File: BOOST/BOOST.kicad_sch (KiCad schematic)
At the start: 274 parts, among them M1 HYG180N10, M10 HYG180N10, M2 HYG180N10, M3 HYG180N10, M4 HYG180N10, M5 HYG180N10, M6 HYG180N10, M7 HYG180N10, M8 HYG180N10, M9 HYG180N10, Q1 PNP, U1 INA241A3, U10 UCC21520, U11 MCP6241, U12 MCP6241, U13 MCP6241, U14 MCP6561, U15 UCC21520, U16 LM2940_12, U17 L7805, U18 L7805, U19 UCC21520, U2 MCP6561, U20 UCC21520, U21 MCP6561, U22 MCP6241, U23 MCP6241, U24 MCP6241, U3 MCP6241, U4 MCP6561, U5 MCP6561, U6 MCP6241, U7 MCP6241, U8 CD4017B, U9 4051

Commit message: added some footprints to kicad schematic
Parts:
- C1, C39, C4, C56, C73, C79, C80, C81: footprint (none) -> Capacitor_SMD:C_1210_3225Metric
- C10, C11, C12, C13, C14, C15, C17, C19, C20, C22, C23, C24, C26, C28, C29, C32, C33, C34, C35, C36, C37, C38, C41, C42, C43, C44, C45, C46, C47, C48, C5, C50, C51, C52, C53, C54, C58, C59, C61, C63, C65, C66, C68, C8, C82, C83, C84, C9: footprint (none) -> Capacitor_SMD:C_0603_1608Metric
- C16, C18, C49, C60, C64, C67: footprint (none) -> Capacitor_SMD:C_1206_3216Metric
- C2, C21, C25, C27, C3, C31, C57, C6, C62, C72, C76: footprint (none) -> Capacitor_SMD:C_0805_2012Metric
- C30, C55, C7: footprint (none) -> Capacitor_SMD:CP_Elec_6.3x5.4
- C40, C69, C85: footprint (none) -> Capacitor_SMD:CP_Elec_10x12.5
- C70, C71, C74, C75, C77, C78, C86, C87, C88: footprint (none) -> Capacitor_SMD:CP_Elec_10x10.5
- D1, D10, D11, D12, D13, D14, D15, D2, D20, D21, D22, D24, D3, D4, D5, D6, D7, D8, D9: footprint (none) -> Diode_SMD:D_SOD-123
- D19: footprint (none) -> Diode_SMD:D_SMC
- D23, D25, D26: footprint (none) -> Diode_SMD:D_SOD-323
- Q1: footprint (none) -> Package_TO_SOT_SMD:SOT-23
- R1, R52, R53, R7: footprint (none) -> Resistor_SMD:R_2512_6332Metric
- R10, R11, R13, R16, R17, R18, R19, R2, R20, R22, R23, R26, R27, R28, R29, R3, R31, R32, R33, R34, R36, R37, R38, R39, R4, R40, R41, R42, R44, R45, R46, R47, R49, R5, R50, R51, R54, R55, R56, R57, R58, R6, R61, R63, R64, R65, R66, R67, R68, R69, R71, R73, R74, R75, R76, R77, R78, R79, R8, R80, R81, R82, R83, R84, R85, R88, R89, R90, R91, R92, R93, R95, R96, R97, R98: footprint (none) -> Resistor_SMD:R_0603_1608Metric
- R14, R15, R21, R25, R35, R43, R48, R59, R60, R70, R72, R86, R87, R9, R94: footprint (none) -> Resistor_SMD:R_0805_2012Metric
- U1: footprint (none) -> Package_SO:SOIC-8_3.9x4.9mm_P1.27mm
- U10, U15, U19, U20: footprint (none) -> Package_SO:SOIC-16W_7.5x10.3mm_P1.27mm
- U11, U12, U13, U14, U2, U21, U22, U23, U24, U3, U4, U5, U6, U7: footprint (none) -> Package_TO_SOT_SMD:SOT-23-5
- U16: footprint (none) -> Package_TO_SOT_SMD:TO-263-3_TabPin2
- U17, U18: footprint (none) -> Package_TO_SOT_SMD:SOT-89-3
- U8, U9: footprint (none) -> Package_SO:SOIC-16_3.9x9.9mm_P1.27mm
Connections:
- net .1Vref_1: now also D26.1 (-), U3.3 (In+); no longer D26.2 (-), U3.1 (In+)
- net .1Vref_2: now also D25.1 (-), U7.3 (In+); no longer D25.2 (-), U7.1 (In+)
- net .1Vref_3: now also D23.1 (-), U13.3 (In+); no longer D23.2 (-), U13.1 (In+)
- net 0: now also D19.2 (+), Q1.3 (C), U11.2 (V-), U12.2 (V-), U13.2 (V-), U14.2 (V-), U16.2 (GND), U19.15 (VSSA), U2.2 (V-), U21.2 (V-), U22.2 (V-), U23.2 (V-), U24.2 (V-), U3.2 (V-), U4.2 (V-), U5.2 (V-), U6.2 (V-), U7.2 (V-); no longer D19.1 (+), Q1.1 (C), U11.4 (V-), U12.4 (V-), U13.4 (V-), U14.4 (V-), U16.3 (GND), U19.12 (VSSB), U2.4 (V-), U21.4 (V-), U22.4 (V-), U23.4 (V-), U24.4 (V-), U3.4 (V-), U4.4 (V-), U5.4 (V-), U6.4 (V-), U7.4 (V-)
- net 0A_hi: now also U2.1 (OUT); no longer U2.5 (OUT)
- net 0err_hi: now also D1.2 (+), D3.1 (-), U4.1 (OUT); no longer D1.1 (+), D3.2 (-), U4.5 (OUT)
- net 10: now also U8.11 (Q9); no longer U8.13 (Q9)
- net 12V: now also D10.2 (+), D21.2 (+), D9.2 (+), U16.3 (OUT), U19.11 (VDDB), U19.16 (VDDA); no longer D10.1 (+), D21.1 (+), D9.1 (+), U16.2 (OUT), U19.10 (VDDB), U19.7 (VDDA)
- net 4: now also U8.15 (MR); no longer U8.1 (MR)
- net 5: now also U8.10 (Q4); no longer U8.8 (Q4)
- net 5V: now also U14.5 (V+), U2.5 (V+), U21.5 (V+), U4.5 (V+), U5.5 (V+), U9.16 (VDD); no longer U14.3 (V+), U2.3 (V+), U21.3 (V+), U4.3 (V+), U5.3 (V+), U9.9 (VDD)
- net 6: now also U8.1 (Q5); no longer U8.9 (Q5)
- net 7: now also U8.5 (Q6); no longer U8.10 (Q6)
- net 8: now also U8.6 (Q7); no longer U8.11 (Q7)
- net 9: now also U8.9 (Q8); no longer U8.12 (Q8)
- net Current: now also U2.4 (In-), U5.3 (In+); no longer U2.2 (In-), U5.1 (In+)
- net GATE_M1: now also D12.2 (+), M1.1 (G); no longer D12.1 (+), M1.2 (G)
- net GATE_M2: now also D11.2 (+), M2.1 (G); no longer D11.1 (+), M2.2 (G)
- net GATE_M3: now also D14.2 (+), M3.1 (G); no longer D14.1 (+), M3.2 (G)
- net GATE_M4: now also D13.2 (+), M4.1 (G); no longer D13.1 (+), M4.2 (G)
- net GATE_M5: now also D22.2 (+), M5.1 (G); no longer D22.1 (+), M5.2 (G)
- net GATE_M6: now also D8.2 (+), M6.1 (G); no longer D8.1 (+), M6.2 (G)
- net GATE_M7: now also D2.2 (+), M7.1 (G); no longer D2.1 (+), M7.2 (G)
- net LX: now also D19.1 (-), M1.2 (D), M5.2 (D), M6.2 (D), M7.2 (D); no longer D19.2 (-), M1.1 (D), M5.1 (D), M6.1 (D), M7.1 (D)
- net OUT_1_ENA: now also U8.3 (Q0), U9.11 (A); no longer U8.4 (Q0), U9.14 (A)
- net OUT_2_ENA: now also U8.2 (Q1), U9.10 (B); no longer U8.5 (Q1), U9.15 (B)
- net OUT_3_ENA: now also U8.4 (Q2), U9.9 (C); no longer U8.6 (Q2), U9.16 (C)
- net Out-: now also D15.2 (+), U8.13 (CPN); no longer D15.1 (+), U8.2 (CPN)
- net Output1_drain: now also D16.1 (-), M10.2 (D); no longer D16.2 (-), M10.1 (D)
- net Output2_drain: now also D18.1 (-), M9.2 (D); no longer D18.2 (-), M9.1 (D)
- net Output3_drain: now also D17.1 (-), M8.2 (D); no longer D17.2 (-), M8.1 (D)
- net Reset_raw: now also U5.1 (OUT); no longer U5.5 (OUT)
- net V_err: now also U4.4 (In-), U5.4 (In-); no longer U4.2 (In-), U5.2 (In-)
- net Verr1: now also U9.13 (IO0), U9.14 (IO1); no longer U9.11 (IO1), U9.12 (IO0)
- net Verr2: now also U9.15 (IO2); no longer U9.10 (IO2)
- net Voltage_err_1: now also U3.1 (OUT); no longer U3.5 (OUT)
- net Voltage_err_2: now also U7.1 (OUT); no longer U7.5 (OUT)
- net Voltage_err_3: now also U13.1 (OUT); no longer U13.5 (OUT)
- net Vout_1: now also D16.2 (+), M2.2 (D); no longer D16.1 (+), M2.1 (D)
- net Vout_2: now also D18.2 (+), M3.2 (D); no longer D18.1 (+), M3.1 (D)
- net Vout_3: now also D17.2 (+), M4.2 (D); no longer D17.1 (+), M4.1 (D)
- net analog_5V: now also U11.5 (V+), U12.5 (V+), U13.5 (V+), U22.5 (V+), U23.5 (V+), U24.5 (V+), U3.5 (V+), U6.5 (V+), U7.5 (V+); no longer U11.3 (V+), U12.3 (V+), U13.3 (V+), U22.3 (V+), U23.3 (V+), U24.3 (V+), U3.3 (V+), U6.3 (V+), U7.3 (V+)
- net low_error_timeout: now also D6.1 (-), U14.1 (OUT), U8.14 (CP); no longer D6.2 (-), U14.5 (OUT), U8.3 (CP)
- net m2_source: now also U15.9 (VSSB); no longer U15.12 (VSSB)
- net m3_source: now also U10.9 (VSSB); no longer U10.12 (VSSB)
- net m4_source: now also U20.15 (VSSA); no longer U20.12 (VSSB)
- net set-: now also D6.2 (+); no longer D6.1 (+)
- net at R31.1, R32.2: now also U7.4 (In-); no longer U7.2 (In-)
- net at R59.2, R74.2: now also D22.1 (-), U20.10 (VOUTB); no longer D22.2 (-), U20.11 (VOUTB)
- net at C68.1, R96.2, R97.1: now also U24.3 (In+); no longer U24.1 (In+)
- net at R67.2, R68.1, R69.1: now also U14.3 (In+); no longer U14.1 (In+)
- net at C16.1, C50.1, R48.2: now also U10.11 (VDDB), U10.16 (VDDA); no longer U10.10 (VDDB), U10.7 (VDDA)
- net at C16.2, C50.2: now also U10.15 (VSSA); no longer U10.9 (VSSA)
- net at C45.1, R57.1, R58.2: now also U11.3 (In+); no longer U11.1 (In+)
- net at M10.3 (S), R52.1: now also U11.4 (In-); no longer U11.2 (In-)
- net at R56.2: now also U11.1 (OUT); no longer U11.5 (OUT)
- net at A14.6 (_Q), R80.2: now also D20.2 (+); no longer D20.1 (+)
- net at R22.1: now also M8.1 (G); no longer M8.2 (G)
- net at M8.3 (S), R7.1: now also U6.4 (In-); no longer U6.2 (In-)
- net at C65.1, R91.2, R92.1: now also U23.3 (In+); no longer U23.1 (In+)
- net at C67.1, R98.1, S3.2 (B): now also U24.4 (In-); no longer U24.2 (In-)
- net at C67.2, R98.2: now also D26.2 (+), U24.1 (OUT); no longer D26.1 (+), U24.5 (OUT)
- net at C44.1, R54.1, R55.2: now also U12.3 (In+); no longer U12.1 (In+)
- net at C14.1, R66.2: now also Q1.2 (E), U14.4 (In-); no longer Q1.3 (E), U14.2 (In-)
- net at R82.2, R85.1, R86.2: now also U21.3 (In+); no longer U21.1 (In+)
- net at R48.1: now also D9.1 (-); no longer D9.2 (-)
- net at C41.1, R10.1, R29.2: now also U6.3 (In+); no longer U6.1 (In+)
- net at R22.2: now also U6.1 (OUT); no longer U6.5 (OUT)
- net at R65.2: now also D3.2 (+); no longer D3.1 (+)
- net at C49.1, R90.1, S1.2 (B): now also U22.4 (In-); no longer U22.2 (In-)
- net at C49.2, R90.2: now also D23.2 (+), U22.1 (OUT); no longer D23.1 (+), U22.5 (OUT)
- net at R21.1: now also D10.1 (-); no longer D10.2 (-)
- net at R15.1, R5.2: now also D12.1 (-), U19.14 (VOUTA); no longer D12.2 (-), U19.8 (VOUTA)
- net at A3.6 (_Q), R78.2: now also D7.2 (+); no longer D7.1 (+)
- net at R83.1, R84.2: now also U21.4 (In-); no longer U21.2 (In-)
- net at R11.2, R16.1, R17.1: now also U2.3 (In+); no longer U2.1 (In+)
- net at R47.2, R73.2: now also D13.1 (-), U20.14 (VOUTA); no longer D13.2 (-), U20.8 (VOUTA)
- net at C60.1, C61.1, R72.2: now also U20.11 (VDDB), U20.16 (VDDA); no longer U20.10 (VDDB), U20.7 (VDDA)
- net at C64.1, R93.1, S2.2 (B): now also U23.4 (In-); no longer U23.2 (In-)
- net at C64.2, R93.2: now also D25.2 (+), U23.1 (OUT); no longer D25.1 (+), U23.5 (OUT)
- net at A20.1 (in), R64.2: now also D5.1 (-); no longer D5.2 (-)
- net at R18.2, R19.1, R20.1: now also U4.3 (In+); no longer U4.1 (In+)
- net at R39.1, R40.2: now also U13.4 (In-); no longer U13.2 (In-)
- net at A6.1 (in), R79.2: now also D7.1 (-); no longer D7.2 (-)
- net at R50.1: now also M9.1 (G); no longer M9.2 (G)
- net at R50.2: now also U12.1 (OUT); no longer U12.5 (OUT)
- net at M9.3 (S), R53.1: now also U12.4 (In-); no longer U12.2 (In-)
- net at C18.1, C51.1, R21.2: now also U15.11 (VDDB), U15.16 (VDDA); no longer U15.10 (VDDB), U15.7 (VDDA)
- net at C18.2, C51.2: now also U15.15 (VSSA); no longer U15.9 (VSSA)
- net at A7.6 (_Q), R63.2: now also D5.2 (+); no longer D5.1 (+)
- net at C59.1, R44.2, R89.1: now also U22.3 (In+); no longer U22.1 (In+)
- net at R2.1, R3.2: now also U3.4 (In-); no longer U3.2 (In-)
- net at R56.1: now also M10.1 (G); no longer M10.2 (G)
- net at C15.1, R71.1: now also D4.1 (-); no longer D4.2 (-)
- net at A13.1 (in), R81.2: now also D20.1 (-); no longer D20.2 (-)
- net at R72.1: now also D21.1 (-); no longer D21.2 (-)
- net at R77.2: now also U19.10 (VOUTB); no longer U19.11 (VOUTB)
- new net: A17.1 (in), D1.1 (-), D15.1 (-), D24.1 (-), R26.1
- new net: D24.2 (+), R86.1, U21.1 (OUT)
- new net: D8.1 (-), R70.1, U10.10 (VOUTB)
- new net: D14.1 (-), R23.1, U10.14 (VOUTA)
- new net: D2.1 (-), R60.1, U15.10 (VOUTB)
- new net: D4.2 (+), Q1.1 (B), R65.1
- new net: D11.1 (-), R13.2, U15.14 (VOUTA)

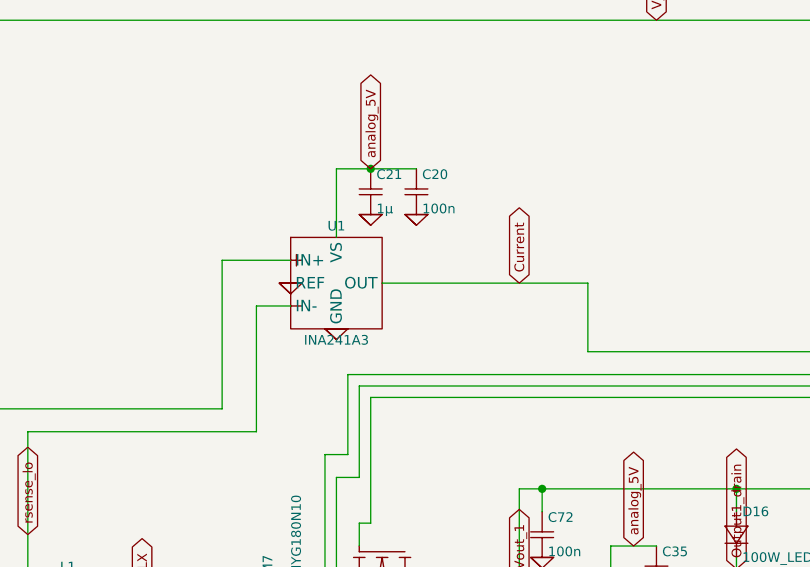
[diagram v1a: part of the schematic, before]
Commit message: added ina current sense thing
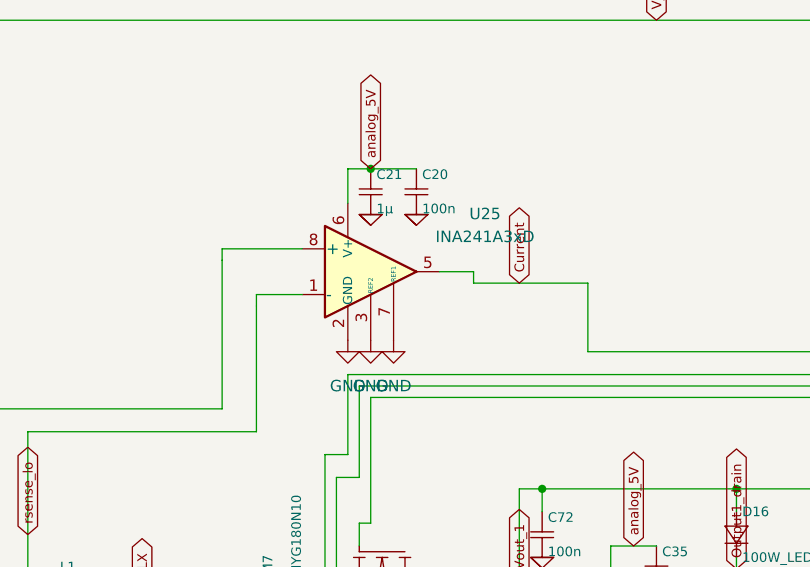
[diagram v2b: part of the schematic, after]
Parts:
- removed U1: INA241A3, Package_SO:SOIC-8_3.9x4.9mm_P1.27mm, symbol ltspice:INA241A3
- added U25: INA241A3xD, Package_SO:SOIC-8_3.9x4.9mm_P1.27mm, symbol Amplifier_Current:INA241A3xD
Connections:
- net Current: now also U25.5
- net Vin: now also U25.8 (+)
- net analog_5V: now also U25.6 (V+)
- net rsense_lo: now also U25.1 (-)
- new net GND: U25.2 (GND), U25.3 (REF2), U25.4 (GND), U25.7 (REF1)

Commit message: added more models
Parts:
- removed C2: 1µ, Capacitor_SMD:C_0805_2012Metric, symbol ltspice:cap
- removed C5: 100n, Capacitor_SMD:C_0603_1608Metric, symbol ltspice:cap
- removed R5, R77: 10k, Resistor_SMD:R_0603_1608Metric, symbol ltspice:res
- removed U10, U19, U20: UCC21520, Package_SO:SOIC-16W_7.5x10.3mm_P1.27mm, symbol ltspice:UCC21520
- removed U17, U18: L7805, Package_TO_SOT_SMD:SOT-89-3, symbol ltspice:L7805
- removed U8: CD4017B, Package_SO:SOIC-16_3.9x9.9mm_P1.27mm, symbol ltspice:CD4017B
- removed U9: 4051, Package_SO:SOIC-16_3.9x9.9mm_P1.27mm, symbol ltspice:CD4051B
- added C89: 1µ, Capacitor_SMD:C_0805_2012Metric, symbol ltspice:cap
- added C90: 100n, Capacitor_SMD:C_0603_1608Metric, symbol ltspice:cap
- added U1, U17: L78L05_SOT89, Package_TO_SOT_SMD:SOT-89-3, symbol Regulator_Linear:L78L05_SOT89
- added U10, U19, U8: UCC21520DW, Package_SO:SOIC-16W_7.5x10.3mm_P1.27mm, symbol Driver_FET:UCC21520DW
- added U18: 4017, symbol 4xxx:4017
- added U20: 74HC14, symbol 74xx:74HC14
- added U26: MCP4451-xxxx-ST, Package_SO:TSSOP-20_4.4x6.5mm_P0.65mm, symbol Potentiometer_Digital:MCP4451-xxxx-ST
- added U27: 74HC00, symbol 74xx:74HC00
- added U28: 74HC4051, symbol 74xx:74HC4051
- added U9: MCP6561-OT, Package_TO_SOT_SMD:SOT-23-5, symbol Comparator:MCP6561-OT
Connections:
- net M1_ON is gone; now on net 5V: A1.4 (d), A17.2 (_Q)
- net 0: now also C89.1, C90.2
- net 12V: now also U19.11 (VDDB), U19.16 (VDDA)
- net 5V: now also C89.2, C90.1, U10.3 (VCCI), U10.6 (DT), U10.8 (VCCI), U17.1 (OUT), U18.16 (VDD), U19.1 (INA), U19.3 (VCCI), U19.6 (DT), U19.8 (VCCI), U28.16 (VCC), U8.3 (VCCI), U8.6 (DT), U8.8 (VCCI)
- net GND: now also U10.4 (GND), U10.5 (DIS), U18.8 (VSS), U19.14 (VSSA), U19.2 (INB), U19.4 (GND), U19.5 (DIS), U19.9 (VSSB), U28.6 (~{E}), U28.7 (VEE), U28.8 (GND), U8.4 (GND), U8.5 (DIS)
- net Out-: now also U18.13 (CKEN)
- net V_err: now also U28.3 (A)
- net Verr1: now also U28.13 (A0), U28.14 (A1)
- net Verr2: now also U28.15 (A2)
- net Verr3: now also U28.1 (A4)
- net Vin: now also U1.3 (IN), U17.3 (IN)
- net analog_5V: now also U1.1 (OUT)
- net ena_out_2: now also U10.2 (INB)
- net ena_out_3: now also U8.2 (INB)
- net low_error_timeout: now also U18.14 (CLK)
- net m3_source: now also C16.2, C50.2, U10.14 (VSSA), U10.9 (VSSB)
- net m4_source: now also U8.14 (VSSA), U8.9 (VSSB)
- net out_2_on: now also U10.1 (INA)
- net out_3_on: now also U8.1 (INA)
- net at D22.1 (-), R59.2, R74.2: now also U8.10 (OUTB)
- net at D8.1 (-), R70.1: now also U10.10 (OUTB)
- net at C16.1, C50.1, R48.2: now also U10.11 (VDDB), U10.16 (VDDA)
- net at D14.1 (-), R23.1: now also U10.15 (OUTA)
- net at D13.1 (-), R47.2, R73.2: now also U8.15 (OUTA)
- net at C60.1, C61.1, R72.2: now also U8.11 (VDDB), U8.16 (VDDA)
- net OUT_1_ENA: no longer names the net of A14.2 (b)
- net OUT_1_ENA: now also U18.1 (Q5), U28.11 (S0)
- net OUT_2_ENA: no longer names the net of A3.2 (b)
- net OUT_2_ENA: now also U18.2 (Q1), U28.10 (S1)
- net OUT_3_ENA: no longer names the net of A7.2 (b)
- net OUT_3_ENA: now also U18.3 (Q0), U28.9 (S2)
- new net: U18.15 (Reset), U18.4 (Q2)
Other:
- moved on the sheet: C12, C31, C48, C54, C57, C58, C62, D14, D8, R23, R49, R70

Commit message: added more models
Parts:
- removed C27: 1µ, Capacitor_SMD:C_0805_2012Metric, symbol ltspice:cap
- removed C47: 100n, Capacitor_SMD:C_0603_1608Metric, symbol ltspice:cap
- removed U15: UCC21520, Package_SO:SOIC-16W_7.5x10.3mm_P1.27mm, symbol ltspice:UCC21520
- added C91: 1µ, Capacitor_SMD:C_0805_2012Metric, symbol ltspice:cap
- added C92: 100n, Capacitor_SMD:C_0603_1608Metric, symbol ltspice:cap
- added R62: 10k, Resistor_SMD:R_0603_1608Metric, symbol ltspice:res
- added U15: UCC21520DW, Package_SO:SOIC-16W_7.5x10.3mm_P1.27mm, symbol Driver_FET:UCC21520DW
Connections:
- net 0: now also C91.1, C92.2
- net 5V: now also C91.2, C92.1, U15.3 (VCCI), U15.6 (DT), U15.8 (VCCI); no longer A1.4 (d), A17.2 (_Q), U19.1 (INA)
- net GND: now also R62.2, U15.4 (GND), U15.5 (DIS)
- net M2_ON: now also U15.1 (INA)
- net ena_out_1: now also U15.2 (INB)
- net m2_source: now also C18.2, C51.2, U15.14 (VSSA), U15.9 (VSSB)
- net at D2.1 (-), R60.1: now also U15.10 (OUTB)
- net at D12.1 (-), R15.1: now also U19.15 (OUTA)
- net at D11.1 (-), R13.2: now also U15.15 (OUTA)
- net at C18.1, C51.1, R21.2: now also U15.11 (VDDB), U15.16 (VDDA)
- net at U19.10 (OUTB): now also R62.1
- new net M1_ON: A1.4 (d), A17.2 (_Q), U19.1 (INA)
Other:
- moved on the sheet: C13, C89, C90, D12, R15

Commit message: trying to fix more stuff
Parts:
- added unit 5 of U101
- added unit 5 of U102
- added unit 5 of U103
- added unit 7 of U104
- added unit 7 of U105
- added unit 5 of U106
- U101: renamed from A1; value Vhigh=5 Vlow=0 Vt=2.5 Td=5n Trise=2n Tfall=2n Rhigh=25 Rlow=15 -> 74HC00; footprint (none) -> Package_SO:SOIC-14_3.9x8.7mm_P1.27mm; symbol ltspice:Digital/and -> ltspice:74HC00_conv
- U101: renamed from A4; value (none) -> 74HC00; footprint (none) -> Package_SO:SOIC-14_3.9x8.7mm_P1.27mm; symbol ltspice:Digital/and -> ltspice:74HC00_conv
- U101: renamed from RESET; value (none) -> 74HC00; footprint (none) -> Package_SO:SOIC-14_3.9x8.7mm_P1.27mm; symbol ltspice:Digital/and -> ltspice:74HC00_conv
- U101: renamed from SET; value (none) -> 74HC00; footprint (none) -> Package_SO:SOIC-14_3.9x8.7mm_P1.27mm; symbol ltspice:Digital/and -> ltspice:74HC00_conv
- U102: renamed from A14; value Vhigh=5 Vlow=0 Vt=2.5 Td=5n Trise=2n Tfall=2n Rhigh=25 Rlow=15 -> 74HC00; footprint (none) -> Package_SO:SOIC-14_3.9x8.7mm_P1.27mm; symbol ltspice:Digital/and -> ltspice:74HC00_conv
- U102: renamed from A3; value Vhigh=5 Vlow=0 Vt=2.5 Td=5n Trise=2n Tfall=2n Rhigh=25 Rlow=15 -> 74HC00; footprint (none) -> Package_SO:SOIC-14_3.9x8.7mm_P1.27mm; symbol ltspice:Digital/and -> ltspice:74HC00_conv
- U102: renamed from A10; value Vhigh=5 Vlow=0 Vt=2.5 Td=5n Trise=2n Tfall=2n Rhigh=25 Rlow=15 -> 74HC00; footprint (none) -> Package_SO:SOIC-14_3.9x8.7mm_P1.27mm; symbol ltspice:Digital/and -> ltspice:74HC00_conv
- U102: renamed from A8; value Vhigh=5 Vlow=0 Vt=2.5 Td=5n Trise=2n Tfall=2n Rhigh=25 Rlow=15 -> 74HC00; footprint (none) -> Package_SO:SOIC-14_3.9x8.7mm_P1.27mm; symbol ltspice:Digital/and -> ltspice:74HC00_conv
- U103: renamed from A7; value Vhigh=5 Vlow=0 Vt=2.5 Td=5n Trise=2n Tfall=2n Rhigh=25 Rlow=15 -> 74HC00; footprint (none) -> Package_SO:SOIC-14_3.9x8.7mm_P1.27mm; symbol ltspice:Digital/and -> ltspice:74HC00_conv
- U103: renamed from A12; value Vhigh=5 Vlow=0 Vt=2.5 Td=5n Trise=2n Tfall=2n Rhigh=25 Rlow=15 -> 74HC00; footprint (none) -> Package_SO:SOIC-14_3.9x8.7mm_P1.27mm; symbol ltspice:Digital/and -> ltspice:74HC00_conv
- U104: renamed from A17; value Vhigh=5 Vlow=0 Vt=2.5 Vh=0.5 Td=4.5n Trise=2n Tfall=2n Rout=20 -> 74HC14; footprint (none) -> Package_SO:SOIC-14_3.9x8.7mm_P1.27mm; symbol ltspice:Digital/schmtinv -> ltspice:74HC14_conv
- U104: renamed from A11; value Vhigh=5 Vlow=0 Vt=2.5 Vh=0.5 Td=4.5n Trise=2n Tfall=2n Rout=20 -> 74HC14; footprint (none) -> Package_SO:SOIC-14_3.9x8.7mm_P1.27mm; symbol ltspice:Digital/schmtinv -> ltspice:74HC14_conv
- U104: renamed from A6; value Vhigh=5 Vlow=0 Vt=2.5 Vh=0.45 Td=15n Trise=7n Tfall=7n Rout=50 -> 74HC14; footprint (none) -> Package_SO:SOIC-14_3.9x8.7mm_P1.27mm; symbol ltspice:Digital/schmtinv -> ltspice:74HC14_conv
- U104: renamed from A18; value Vhigh=5 Vlow=0 Vt=2.5 Vh=0.5 Td=4.5n Trise=2n Tfall=2n Rout=20 -> 74HC14; footprint (none) -> Package_SO:SOIC-14_3.9x8.7mm_P1.27mm; symbol ltspice:Digital/schmtinv -> ltspice:74HC14_conv
- U104: renamed from A2; value Vhigh=5 Vlow=0 Vt=2.5 Vh=0.45 Td=15n Trise=7n Tfall=7n Rout=50 -> 74HC14; footprint (none) -> Package_SO:SOIC-14_3.9x8.7mm_P1.27mm; symbol ltspice:Digital/schmtinv -> ltspice:74HC14_conv
- U104: renamed from A9; value Vhigh=5 Vlow=0 Vt=2.5 Vh=0.5 Td=4.5n Trise=2n Tfall=2n Rout=20 -> 74HC14; footprint (none) -> Package_SO:SOIC-14_3.9x8.7mm_P1.27mm; symbol ltspice:Digital/schmtinv -> ltspice:74HC14_conv
- U105: renamed from A13; value Vhigh=5 Vlow=0 Vt=2.5 Vh=0.45 Td=15n Trise=7n Tfall=7n Rout=50 -> 74HC14; footprint (none) -> Package_SO:SOIC-14_3.9x8.7mm_P1.27mm; symbol ltspice:Digital/schmtinv -> ltspice:74HC14_conv
- U105: renamed from A20; value Vhigh=5 Vlow=0 Vt=2.5 Vh=0.45 Td=15n Trise=7n Tfall=7n Rout=50 -> 74HC14; footprint (none) -> Package_SO:SOIC-14_3.9x8.7mm_P1.27mm; symbol ltspice:Digital/schmtinv -> ltspice:74HC14_conv
- U106: renamed from S1; value AGATE -> CD74HC4066; footprint (none) -> Package_SO:SOIC-14_3.9x8.7mm_P1.27mm; symbol ltspice:sw -> ltspice:CD4066_conv
- U106: renamed from S3; value AGATE -> CD74HC4066; footprint (none) -> Package_SO:SOIC-14_3.9x8.7mm_P1.27mm; symbol ltspice:sw -> ltspice:CD4066_conv
- U106: renamed from S2; value AGATE -> CD74HC4066; footprint (none) -> Package_SO:SOIC-14_3.9x8.7mm_P1.27mm; symbol ltspice:sw -> ltspice:CD4066_conv
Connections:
- net 0: no longer U104.3 (com), U104.3 (com), U104.3 (com), U104.3 (com), U104.3 (com), U104.3 (com), U105.3 (com), U105.3 (com), U106.4 (NC-), U106.4 (NC-), U106.4 (NC-)
- net 0A_hi: now also U101.2 (B); no longer U101.4 (d)
- net 0err_hi: now also U104.11 (A); no longer U104.1 (in)
- net GND: now also U28.12 (A3), U28.2 (A6), U28.4 (A7), U28.5 (A5)
- net M1_ON: now also U101.5 (B); no longer U101.4 (d)
- net M2_ON: now also U104.4 (Y); no longer U104.2 (_Q)
- net Out: now also U101.13 (A), U101.8 (Y); no longer U101.2 (b), U101.6 (_Q)
- net Out-: now also U101.11 (Y), U101.9 (B), U102.1 (A), U102.13 (A), U103.5 (B); no longer U101.4 (d), U101.6 (_Q), U102.2 (b), U102.2 (b), U103.4 (d)
- net RESET-: now also U101.12 (B); no longer U101.4 (d)
- net Reset_raw: now also U101.4 (A); no longer U101.2 (b)
- net VerrGT0: now also U101.1 (A), U102.5 (B), U102.9 (B), U103.2 (B), U104.10 (Y); no longer U101.2 (b), U102.4 (d), U102.4 (d), U103.4 (d), U104.2 (_Q)
- net analog_5V: now also U106.13 (CTRL), U106.5 (CTRL), U106.6 (CTRL); no longer U106.3 (NC+), U106.3 (NC+), U106.3 (NC+)
- net ena_out_1: now also U102.2 (B); no longer U102.4 (d)
- net ena_out_2: now also U102.12 (B), U104.12 (Y); no longer U102.4 (d), U104.2 (_Q)
- net ena_out_3: now also U103.4 (A), U105.4 (Y); no longer U103.2 (b), U105.2 (_Q)
- net out_2_on: now also U104.6 (Y); no longer U104.2 (_Q)
- net out_3_on: now also U104.8 (Y); no longer U104.2 (_Q)
- net set-: now also U101.10 (A); no longer U101.2 (b)
- net at C67.1, R98.1, U24.4 (In-): now also U106.9 (B); no longer U106.2 (B)
- net at D7.2 (+), R78.2: now also U102.8 (Y); no longer U102.6 (_Q)
- net at C64.1, R93.1, U23.4 (In-): now also U106.4 (B); no longer U106.2 (B)
- net at D5.1 (-), R64.2: now also U105.3 (A); no longer U105.1 (in)
- net at D7.1 (-), R79.2: now also U104.13 (A); no longer U104.1 (in)
- net at U18.2 (Q1), U28.10 (S1): now also U102.10 (A); no longer U102.2 (b)
- net at R25.2, R36.1: now also U106.3 (A); no longer U106.1 (A)
- net at R94.2, R95.1: now also U106.8 (A); no longer U106.1 (A)
- net at D5.2 (+), R63.2: now also U103.3 (Y); no longer U103.6 (_Q)
- net at U101.3 (Y): now also R4.2
- net at U103.6 (Y): now also U104.9 (A); no longer U104.1 (in)
- net at U103.1 (A): now also U18.4 (Q2), U28.9 (S2)
- net at U102.3 (Y): now also U104.3 (A)
- net at U18.15 (Reset): now also U18.7 (Q3); no longer U18.4 (Q2)
- new net: U102.4 (A), U18.3 (Q0), U28.11 (S0)
- new net: U102.11 (Y), U104.5 (A)
- now unconnected: U18.1 (Q5)

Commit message: put in stuff to replace ltspice voltage sources
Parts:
- removed IREF1: 2.5, symbol ltspice:voltage
- removed IREF2, IREF3: 2.25, symbol ltspice:voltage
- removed R10: 1800, Resistor_SMD:R_0603_1608Metric, symbol ltspice:res
- removed REFERENCE_V1: 2, symbol ltspice:voltage
- removed REFERENCE_V2, REFERENCE_V3: 3, symbol ltspice:voltage
- added C100, C101, C102: 1n, Capacitor_SMD:C_0603_1608Metric, symbol ltspice:cap
- added C103, C47, C93: 10u, Capacitor_SMD:C_0603_1608Metric, symbol ltspice:cap
- added C94, C95, C96, C97, C98, C99: 100n, Capacitor_SMD:C_0603_1608Metric, symbol ltspice:cap
- added R100, R101, R77: 10k, Resistor_SMD:R_0603_1608Metric, symbol ltspice:res
- added R30: 22k, Resistor_SMD:R_0805_2012Metric, symbol ltspice:res
- added unit 2 of U26
- added unit 3 of U26
- C41, C44, C45: value 100n -> 1n
- R29: value 100 -> 22k; footprint Resistor_SMD:R_0603_1608Metric -> Resistor_SMD:R_0805_2012Metric
- R54: value 1800 -> 1k
- R55, R58: value 100 -> 1k
- R57: value 1800 -> 22k; footprint Resistor_SMD:R_0603_1608Metric -> Resistor_SMD:R_0805_2012Metric
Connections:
- net 0: now also R54.2, R55.2, R58.2, C100.2, C101.2, C102.2, C94.2, C95.2, C96.2, C97.2, C98.2, C99.2; no longer R29.1, R55.1, R58.1
- net 5V: now also U101.14 (VCC), U102.14 (VCC), U103.14 (VCC), U104.14 (VCC), U105.14 (VCC), U106.14 (VDD), C94.1, C95.1, C96.1, C97.1, C98.1, C99.1
- net GND: now also U101.7 (GND), U102.7 (GND), U103.7 (GND), U104.7 (GND), U105.7 (GND), U106.7 (VSS), U26.11 (P0A), U28.13 (A0), C103.2, C47.2, C93.2, U26.10 (P1A), U26.20 (P2A)
- net Verr1: no longer U28.13 (A0)
- net Vref_1: now also C103.1, R101.2
- net Vref_2: now also C93.1, R100.2
- net Vref_3: now also C47.1, R77.2
- net analog_5V: no longer U106.13 (CTRL), U106.5 (CTRL), U106.6 (CTRL)
- net IREF1_input: now reaches C45.1, U11.3 (In+)
- net IREF1_input: now also U26.12 (P0W); no longer R57.1, R58.2
- net IREF2_input: now reaches C44.1, U12.3 (In+)
- net IREF2_input: now also U26.9 (P1W); no longer R54.1, R55.2
- net at U26.13 (P0B): now also R29.2, R54.1, C100.1
- net IREF3_input: now reaches C41.1, U6.3 (In+)
- net IREF3_input: now also U26.19 (P2W); no longer R29.2
- net at R57.2: now also R58.1, C102.1, U26.18 (P2B)
- new net: C101.1, R30.2, R55.1, U26.8 (P1B)
- new net IREF1: R29.1, U106.6 (CTRL)
- new net IREF2: R30.1, U106.5 (CTRL)
- new net IREF3: R57.1, U106.13 (CTRL)
- new net Vref_1_arduino: R101.1
- new net Vref_2_arduino: R100.1
- new net Vref_3_arduino: R77.1
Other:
- moved on the sheet: U26A

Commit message: put in stuff to replace ltspice voltage sources
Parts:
- removed L2: 0.8µ, symbol ltspice:ind
- removed R99: 0.012, symbol ltspice:res
- removed V1: 14, symbol ltspice:voltage
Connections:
- net 0 is gone; now on net GND: C1.2, C10.1, C100.2, C101.2, C102.2, C11.1, C12.2, C13.1, C14.2, C15.2, C17.1, C19.2, C20.2, C21.2, C22.2, C23.2, C24.2, C25.2, C26.2, C28.2, C29.2, C3.2, C30.2, C31.2, C32.2, C33.2, C34.2, C35.2, C36.1, C37.1, C38.1, C39.2, C4.2, C40.2, C41.2, C42.2, C43.2, C44.2, C45.2, C46.2, C48.2, C52.2, C53.1, C54.2, C55.2, C56.2, C57.1, C58.2, C59.2, C6.2, C62.1, C63.2, C65.2, C66.2, C68.2, C69.2, C7.2, C70.2, C71.2, C72.2, C73.2, C74.2, C75.2, C76.2, C77.2, C78.2, C79.2, C8.1, C80.2, C81.2, C82.2, C83.2, C84.2, C85.2, C86.2, C87.2, C88.2, C89.1, C9.1, C90.2, C91.1, C92.2, C94.2, C95.2, C96.2, C97.2, C98.2, C99.2, D19.2 (+), M1.3 (S), Q1.3 (C), R14.2, R16.2, R19.2, R28.1, R34.2, R36.2, R38.1, R42.2, R46.1, R52.2, R53.2, R54.2, R55.2, R58.2, R68.2, R7.2, R8.2, R83.2, R85.2, R88.2, R89.2, R92.2, R95.2, R97.2, U11.2 (V-), U12.2 (V-), U13.2 (V-), U14.2 (V-), U16.2 (GND), U2.2 (V-), U21.2 (V-), U22.2 (V-), U23.2 (V-), U24.2 (V-), U3.2 (V-), U4.2 (V-), U5.2 (V-), U6.2 (V-), U7.2 (V-)
- net GND: now also U1.2 (GND), U17.2 (GND)
